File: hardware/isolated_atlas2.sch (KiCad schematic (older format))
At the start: 17 parts, among them J13 CONN_01x02, J14 CONN_01x02, J401 CONN_01X02, P4 ATLAS_PH_PROBE, U401 ADM3260, U402 ATLAS_PH

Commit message: Add orientation indicator to SWD fp.
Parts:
- J13, J14: Critical (none) -> (none); MFN (none) -> (none); MFP (none) -> (none); Notes (none) -> (none); Package (none) -> (none); SPN1 (none) -> (none); Source (none) -> ANY; Subsystem (none) -> (none); Supplier1 (none) -> (none)
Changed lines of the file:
@@
+	1    0    0    -1
+$EndComp
+$Comp
+L conservify:CONN_01x02 J?
+U 1 1 5C0ECD1F
+P 8950 4150
+AR Path="/594C282A/5C0ECD1F" Ref="J?"  Part="1"
+AR Path="/594C282D/5C0ECD1F" Ref="J13"  Part="1"
+F 0 "J13" H 9029 4142 50  0000 L CNN
+F 1 "CONN_01x02" H 9029 4051 50  0000 L CNN
+F 2 "conservify:TP_Pads_D1.5mm_1x2" H 8950 4150 50  0001 C CNN
+F 3 "" H 8950 4150 50  0001 C CNN
+F 4 " " H 9029 4242 50  0001 C CNN "Critical"
+F 5 " " H 9029 4242 50  0001 C CNN "MFN"
+F 6 " " H 9029 4242 50  0001 C CNN "MFP"
+F 7 " " H 9029 4242 50  0001 C CNN "Notes"
+F 8 " " H 9029 4242 50  0001 C CNN "Package"
+F 9 " " H 9029 4242 50  0001 C CNN "SPN1"
+F 10 "ANY" H 9029 4242 50  0001 C CNN "Source"
+F 11 " " H 9029 4242 50  0001 C CNN "Subsystem"
+F 12 " " H 9029 4242 50  0001 C CNN "Supplier1"
+	1    8950 4150
+	1    0    0    -1
+$EndComp
+$Comp
+L conservify:CONN_01x02 J?
+U 1 1 5C0ECD26
+P 8950 4400
+AR Path="/594C282A/5C0ECD26" Ref="J?"  Part="1"
+AR Path="/594C282D/5C0ECD26" Ref="J14"  Part="1"
+F 0 "J14" H 9029 4392 50  0000 L CNN
+F 1 "CONN_01x02" H 9029 4301 50  0000 L CNN
+F 2 "conservify:TP_Pads_D1.5mm_1x2" H 8950 4400 50  0001 C CNN
+F 3 "" H 8950 4400 50  0001 C CNN
+F 4 " " H 9029 4492 50  0001 C CNN "Critical"
+F 5 " " H 9029 4492 50  0001 C CNN "MFN"
+F 6 " " H 9029 4492 50  0001 C CNN "MFP"
+F 7 " " H 9029 4492 50  0001 C CNN "Notes"
+F 8 " " H 9029 4492 50  0001 C CNN "Package"
+F 9 " " H 9029 4492 50  0001 C CNN "SPN1"
+F 10 "ANY" H 9029 4492 50  0001 C CNN "Source"
+F 11 " " H 9029 4492 50  0001 C CNN "Subsystem"
+F 12 " " H 9029 4492 50  0001 C CNN "Supplier1"
+	1    8950 4400
 	1    0    0    -1
 $EndComp
@@
 Text Label 9450 2900 0    60   ~ 0
 PH_PGND
+Text Label 8350 4500 0    60   ~ 0
+ISO_GND
+Text Label 8350 4400 0    60   ~ 0
+ISO_VCC
+Text Label 8350 4150 0    60   ~ 0
+ISO_SCL
+Text Label 8350 4250 0    60   ~ 0
+ISO_SDA
 Wire Wire Line
 	5200 3300 5350 3300
@@
 Wire Wire Line
 	6900 2500 7400 2500
+Wire Wire Line
+	8350 4150 8750 4150
+Wire Wire Line
+	8750 4250 8350 4250
+Wire Wire Line
+	8350 4400 8750 4400
+Wire Wire Line
+	8750 4500 8350 4500
 Connection ~ 5350 3500
 Connection ~ 5350 3400
@@
 NoConn ~ 3650 3000
 NoConn ~ 5200 3000
-Text Label 8350 4500 0    60   ~ 0
-ISO_GND
-Text Label 8350 4400 0    60   ~ 0
-ISO_VCC
-Text Label 8350 4150 0    60   ~ 0
-ISO_SCL
-Text Label 8350 4250 0    60   ~ 0
-ISO_SDA
-Wire Wire Line
-	8350 4150 8750 4150
-Wire Wire Line
-	8750 4250 8350 4250
-Wire Wire Line
-	8350 4400 8750 4400
-Wire Wire Line
-	8750 4500 8350 4500
-$Comp
-L conservify:CONN_01x02 J?
-U 1 1 5C0ECD1F
-P 8950 4150
-AR Path="/594C282A/5C0ECD1F" Ref="J?"  Part="1"
-AR Path="/594C282D/5C0ECD1F" Ref="J13"  Part="1"
-F 0 "J13" H 9029 4142 50  0000 L CNN
-F 1 "CONN_01x02" H 9029 4051 50  0000 L CNN
-F 2 "conservify:TP_Pads_D1.5mm_1x2" H 8950 4150 50  0001 C CNN
-F 3 "" H 8950 4150 50  0001 C CNN
-	1    8950 4150
-	1    0    0    -1
-$EndComp
-$Comp
-L conservify:CONN_01x02 J?
-U 1 1 5C0ECD26
-P 8950 4400
-AR Path="/594C282A/5C0ECD26" Ref="J?"  Part="1"
-AR Path="/594C282D/5C0ECD26" Ref="J14"  Part="1"
-F 0 "J14" H 9029 4392 50  0000 L CNN
-F 1 "CONN_01x02" H 9029 4301 50  0000 L CNN
-F 2 "conservify:TP_Pads_D1.5mm_1x2" H 8950 4400 50  0001 C CNN
-F 3 "" H 8950 4400 50  0001 C CNN
-	1    8950 4400
-	1    0    0    -1
-$EndComp
 $EndSCHEMATC

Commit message: Started transition to 4 layer board
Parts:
- removed J13, J14: CONN_01x02, conservify:TP_Pads_D1.5mm_1x2, symbol conservify:CONN_01x02
- C401, C402, C403, C404, C405, C406: symbol conservify:CAPACITOR_CERAMIC -> fk-atlas-rescue:CAPACITOR_CERAMIC-conservify
- J401: symbol conservify:CONN_01x02 -> fk-atlas-rescue:CONN_01x02-conservify
- P4: symbol conservify:ATLAS_WATER_PROBE -> fk-atlas-rescue:ATLAS_WATER_PROBE-conservify
- R401, R402, R403, R404, R405: symbol conservify:R -> fk-atlas-rescue:R-conservify
- U401: symbol conservify:ADM3260 -> fk-atlas-rescue:ADM3260-conservify
- U402: footprint conservify:ATLAS_SENSOR_BOARD_OEM -> conservify:ATLAS_SENSOR_BOARD_COMBO; symbol conservify:ATLAS_SENSOR -> fk-atlas-rescue:ATLAS_SENSOR-conservify
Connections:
- wire segments 82 -> 78
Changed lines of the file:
@@
 $EndDescr
 $Comp
-L conservify:ADM3260 U401
+L fk-atlas-rescue:ADM3260-conservify U401
 U 1 1 594C2CF1
 P 4400 2900
@@
 $EndComp
 $Comp
-L conservify:CAPACITOR_CERAMIC C403
+L fk-atlas-rescue:CAPACITOR_CERAMIC-conservify C403
 U 1 1 594C2CF4
 P 5650 3800
@@
 $EndComp
 $Comp
-L conservify:CAPACITOR_CERAMIC C404
+L fk-atlas-rescue:CAPACITOR_CERAMIC-conservify C404
 U 1 1 594C2CF8
 P 5650 4100
@@
 $EndComp
 $Comp
-L conservify:CAPACITOR_CERAMIC C405
+L fk-atlas-rescue:CAPACITOR_CERAMIC-conservify C405
 U 1 1 594C2CFB
 P 5650 4400
@@
 $EndComp
 $Comp
-L conservify:CAPACITOR_CERAMIC C406
+L fk-atlas-rescue:CAPACITOR_CERAMIC-conservify C406
 U 1 1 594C2CFF
 P 5650 4650
@@
 $EndComp
 $Comp
-L conservify:CAPACITOR_CERAMIC C401
+L fk-atlas-rescue:CAPACITOR_CERAMIC-conservify C401
 U 1 1 594C2D03
 P 2900 3800
@@
 $EndComp
 $Comp
-L conservify:CAPACITOR_CERAMIC C402
+L fk-atlas-rescue:CAPACITOR_CERAMIC-conservify C402
 U 1 1 594C2D07
 P 2900 4100
@@
 $EndComp
 $Comp
-L conservify:R R401
+L fk-atlas-rescue:R-conservify R401
 U 1 1 594C2D0B
 P 5650 3300
@@
 $EndComp
 $Comp
-L conservify:R R402
+L fk-atlas-rescue:R-conservify R402
 U 1 1 594C2D10
 P 6250 2700
@@
 $EndComp
 $Comp
-L conservify:R R404
+L fk-atlas-rescue:R-conservify R404
 U 1 1 594C2D14
 P 6700 2700
@@
 $EndComp
 $Comp
-L conservify:R R403
+L fk-atlas-rescue:R-conservify R403
 U 1 1 5948E450
 P 6300 3250
@@
 $EndComp
 $Comp
-L conservify:R R405
+L fk-atlas-rescue:R-conservify R405
 U 1 1 594C2D1B
 P 6800 3250
@@
 $EndComp
 $Comp
-L conservify:VCC #PWR061
+L fk-atlas-rescue:VCC-conservify #PWR061
 U 1 1 594C2D24
 P 2450 3750
@@
 $EndComp
 $Comp
-L conservify:VCC #PWR062
+L fk-atlas-rescue:VCC-conservify #PWR062
 U 1 1 594C2D2A
 P 2450 2350
@@
 $EndComp
 $Comp
-L conservify:ATLAS_SENSOR U402
+L fk-atlas-rescue:ATLAS_SENSOR-conservify U402
 U 1 1 594C2D35
 P 8550 2900
 F 0 "U402" H 8100 2550 60  0000 C CNN
 F 1 "ATLAS_PH" H 8600 2850 60  0000 C CNN
-F 2 "conservify:ATLAS_SENSOR_BOARD_OEM" H 8550 2900 60  0001 C CNN
+F 2 "conservify:ATLAS_SENSOR_BOARD_COMBO" H 8550 2900 60  0001 C CNN
 F 3 "" H 8550 2900 60  0001 C CNN
 F 4 " " H 8100 2650 50  0001 C CNN "Critical"
@@
 $EndComp
 $Comp
-L conservify:CONN_01x02 J401
+L fk-atlas-rescue:CONN_01x02-conservify J401
 U 1 1 59A1BC7D
 P 10100 2900
@@
 $EndComp
 $Comp
-L conservify:ATLAS_WATER_PROBE P4
+L fk-atlas-rescue:ATLAS_WATER_PROBE-conservify P4
 U 1 1 59D2A29B
 P 8800 3600
@@
 $EndComp
 $Comp
-L conservify:PWR_FLAG #FLG0107
+L fk-atlas-rescue:PWR_FLAG-conservify #FLG0107
 U 1 1 5BCC2A39
 P 7400 4900
@@
 F 3 "~" H 7400 4900 50  0001 C CNN
 	1    7400 4900
-	1    0    0    -1
-$EndComp
-$Comp
-L conservify:CONN_01x02 J?
-U 1 1 5C0ECD1F
-P 8950 4150
-AR Path="/594C282A/5C0ECD1F" Ref="J?"  Part="1"
-AR Path="/594C282D/5C0ECD1F" Ref="J13"  Part="1"
-F 0 "J13" H 9029 4142 50  0000 L CNN
-F 1 "CONN_01x02" H 9029 4051 50  0000 L CNN
-F 2 "conservify:TP_Pads_D1.5mm_1x2" H 8950 4150 50  0001 C CNN
-F 3 "" H 8950 4150 50  0001 C CNN
-F 4 " " H 9029 4242 50  0001 C CNN "Critical"
-F 5 " " H 9029 4242 50  0001 C CNN "MFN"
-F 6 " " H 9029 4242 50  0001 C CNN "MFP"
-F 7 " " H 9029 4242 50  0001 C CNN "Notes"
-F 8 " " H 9029 4242 50  0001 C CNN "Package"
-F 9 " " H 9029 4242 50  0001 C CNN "SPN1"
-F 10 "ANY" H 9029 4242 50  0001 C CNN "Source"
-F 11 " " H 9029 4242 50  0001 C CNN "Subsystem"
-F 12 " " H 9029 4242 50  0001 C CNN "Supplier1"
-	1    8950 4150
-	1    0    0    -1
-$EndComp
-$Comp
-L conservify:CONN_01x02 J?
-U 1 1 5C0ECD26
-P 8950 4400
-AR Path="/594C282A/5C0ECD26" Ref="J?"  Part="1"
-AR Path="/594C282D/5C0ECD26" Ref="J14"  Part="1"
-F 0 "J14" H 9029 4392 50  0000 L CNN
-F 1 "CONN_01x02" H 9029 4301 50  0000 L CNN
-F 2 "conservify:TP_Pads_D1.5mm_1x2" H 8950 4400 50  0001 C CNN
-F 3 "" H 8950 4400 50  0001 C CNN
-F 4 " " H 9029 4492 50  0001 C CNN "Critical"
-F 5 " " H 9029 4492 50  0001 C CNN "MFN"
-F 6 " " H 9029 4492 50  0001 C CNN "MFP"
-F 7 " " H 9029 4492 50  0001 C CNN "Notes"
-F 8 " " H 9029 4492 50  0001 C CNN "Package"
-F 9 " " H 9029 4492 50  0001 C CNN "SPN1"
-F 10 "ANY" H 9029 4492 50  0001 C CNN "Source"
-F 11 " " H 9029 4492 50  0001 C CNN "Subsystem"
-F 12 " " H 9029 4492 50  0001 C CNN "Supplier1"
-	1    8950 4400
 	1    0    0    -1
 $EndComp
@@
 Text Label 9450 2900 0    60   ~ 0
 PH_PGND
-Text Label 8350 4500 0    60   ~ 0
-ISO_GND
-Text Label 8350 4400 0    60   ~ 0
-ISO_VCC
-Text Label 8350 4150 0    60   ~ 0
-ISO_SCL
-Text Label 8350 4250 0    60   ~ 0
-ISO_SDA
 Wire Wire Line
 	5200 3300 5350 3300
@@
 Wire Wire Line
 	6900 2500 7400 2500
-Wire Wire Line
-	8350 4150 8750 4150
-Wire Wire Line
-	8750 4250 8350 4250
-Wire Wire Line
-	8350 4400 8750 4400
-Wire Wire Line
-	8750 4500 8350 4500
 Connection ~ 5350 3500
 Connection ~ 5350 3400

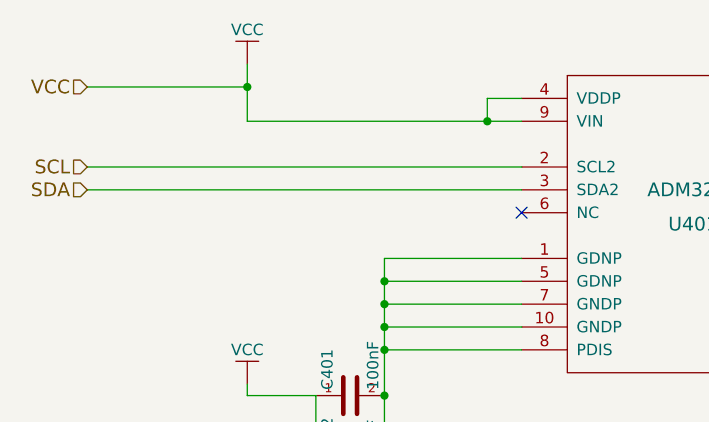
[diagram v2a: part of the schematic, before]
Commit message: Added pull up resistors and a debounce cap for the reset button
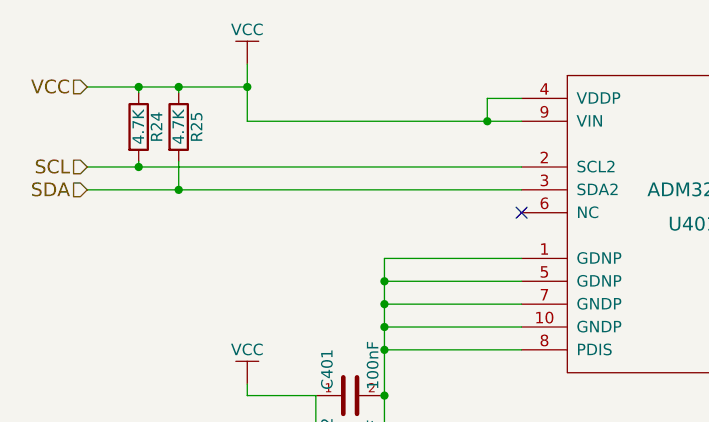
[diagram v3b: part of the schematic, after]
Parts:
- added R24, R25: 4.7K, conservify:RES-0603, symbol fk-atlas-rescue:R-conservify
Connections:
- net SCL: now also R24.2
- net SDA: now also R25.2
- net VCC: now also R24.1, R25.1
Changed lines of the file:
@@
 	2450 3800 2450 3750
 Wire Wire Line
-	1750 2800 3650 2800
+	1750 2800 1975 2800
 Wire Wire Line
-	1750 2900 3650 2900
+	1750 2900 2150 2900
 Wire Wire Line
-	1750 2450 2450 2450
+	1750 2450 1975 2450
 Wire Wire Line
 	5350 5000 7400 5000
@@
 NoConn ~ 3650 3000
 NoConn ~ 5200 3000
+$Comp
+L fk-atlas-rescue:R-conservify R24
+U 1 1 5C7FF88D
+P 1975 2625
+F 0 "R24" V 2055 2625 50  0000 C CNN
+F 1 "4.7K" V 1975 2625 50  0000 C CNN
+F 2 "conservify:RES-0603" V 1905 2625 50  0001 C CNN
+F 3 "" H 1975 2625 50  0001 C CNN
+F 4 " " H 2055 2725 50  0001 C CNN "Critical"
+F 5 "Yageo" H 2055 2725 50  0001 C CNN "MFN"
+F 6 "AF0603JR-074K7L" H 2055 2725 50  0001 C CNN "MFP"
+F 7 " " H 2055 2725 50  0001 C CNN "Notes"
+F 8 " " H 2055 2725 50  0001 C CNN "Package"
+F 9 "ANY" H 2055 2725 50  0001 C CNN "Source"
+F 10 " " H 2055 2725 50  0001 C CNN "Subsystem"
+F 11 "mouser" H 2055 2725 50  0001 C CNN "Supplier1"
+F 12 "0" H 2055 2725 50  0001 C CNN "price"
+F 13 "603-AF0603JR-074K7L" H -4325 -625 50  0001 C CNN "spn1"
+F 14 "mouser" H -4325 -625 50  0001 C CNN "spn2"
+	1    1975 2625
+	1    0    0    -1
+$EndComp
+Wire Wire Line
+	1975 2475 1975 2450
+Connection ~ 1975 2450
+Wire Wire Line
+	1975 2450 2150 2450
+Wire Wire Line
+	1975 2775 1975 2800
+Connection ~ 1975 2800
+Wire Wire Line
+	1975 2800 3650 2800
+$Comp
+L fk-atlas-rescue:R-conservify R25
+U 1 1 5C803402
+P 2150 2625
+F 0 "R25" V 2230 2625 50  0000 C CNN
+F 1 "4.7K" V 2150 2625 50  0000 C CNN
+F 2 "conservify:RES-0603" V 2080 2625 50  0001 C CNN
+F 3 "" H 2150 2625 50  0001 C CNN
+F 4 " " H 2230 2725 50  0001 C CNN "Critical"
+F 5 "Yageo" H 2230 2725 50  0001 C CNN "MFN"
+F 6 "AF0603JR-074K7L" H 2230 2725 50  0001 C CNN "MFP"
+F 7 " " H 2230 2725 50  0001 C CNN "Notes"
+F 8 " " H 2230 2725 50  0001 C CNN "Package"
+F 9 "ANY" H 2230 2725 50  0001 C CNN "Source"
+F 10 " " H 2230 2725 50  0001 C CNN "Subsystem"
+F 11 "mouser" H 2230 2725 50  0001 C CNN "Supplier1"
+F 12 "0" H 2230 2725 50  0001 C CNN "price"
+F 13 "603-AF0603JR-074K7L" H -4150 -625 50  0001 C CNN "spn1"
+F 14 "mouser" H -4150 -625 50  0001 C CNN "spn2"
+	1    2150 2625
+	1    0    0    -1
+$EndComp
+Wire Wire Line
+	2150 2475 2150 2450
+Connection ~ 2150 2450
+Wire Wire Line
+	2150 2450 2450 2450
+Wire Wire Line
+	2150 2775 2150 2900
+Connection ~ 2150 2900
+Wire Wire Line
+	2150 2900 3650 2900
 $EndSCHEMATC
